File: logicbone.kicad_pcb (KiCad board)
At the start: 8 copper layers, 86.4 x 54.6 mm, 234 parts, among them IC1 ECP5UM-CABGA381, IC10 AT25SL128A, IC12 74LVC1G07, IC13 TPS51206, IC14 KSZ9031RNXCA, IC16 NCP349, IC17 NCP110AMX110, IC18 NCP110AMX110, IC19 NCP115AMX250, IC2 DDR3-TFBGA78, IC20 NCP115AMX250, IC3 DDR3-TFBGA78, IC4 MXL7704, IC5 PI6CG18401, IC7 FUSB302-QFN14, IC9 ADC120, J1 NGFF-KEY-E, J2 GCT_USB4110_USBC, J3 ARJM11xx-502, J4 TC2050-IDC-NL, J6 Micro_SD_MEM2075, P8 BB_2x23, P9 BB_2x23, Q1 Q_PMOS_GSD, SW1 SW_SPST, SW2 SW_SPST, Y1 25MHz

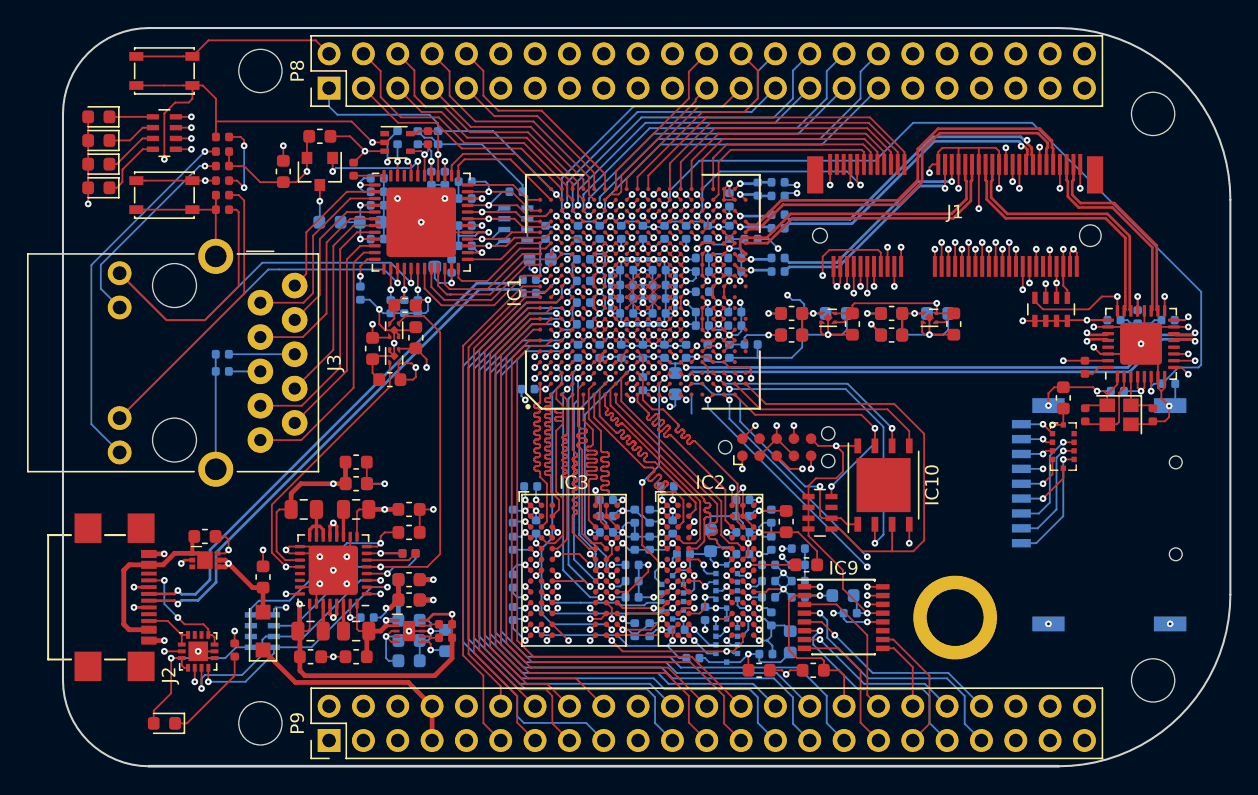
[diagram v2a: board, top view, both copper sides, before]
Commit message: Add a second USB-C port for USB host and SERDES breakout.
Now that the supervisor is gone, we have a bunch more PCB space which
we can use to add a USB-C downstream facing port that can serve as a
USB host and to breakout the extra SERDES channels.
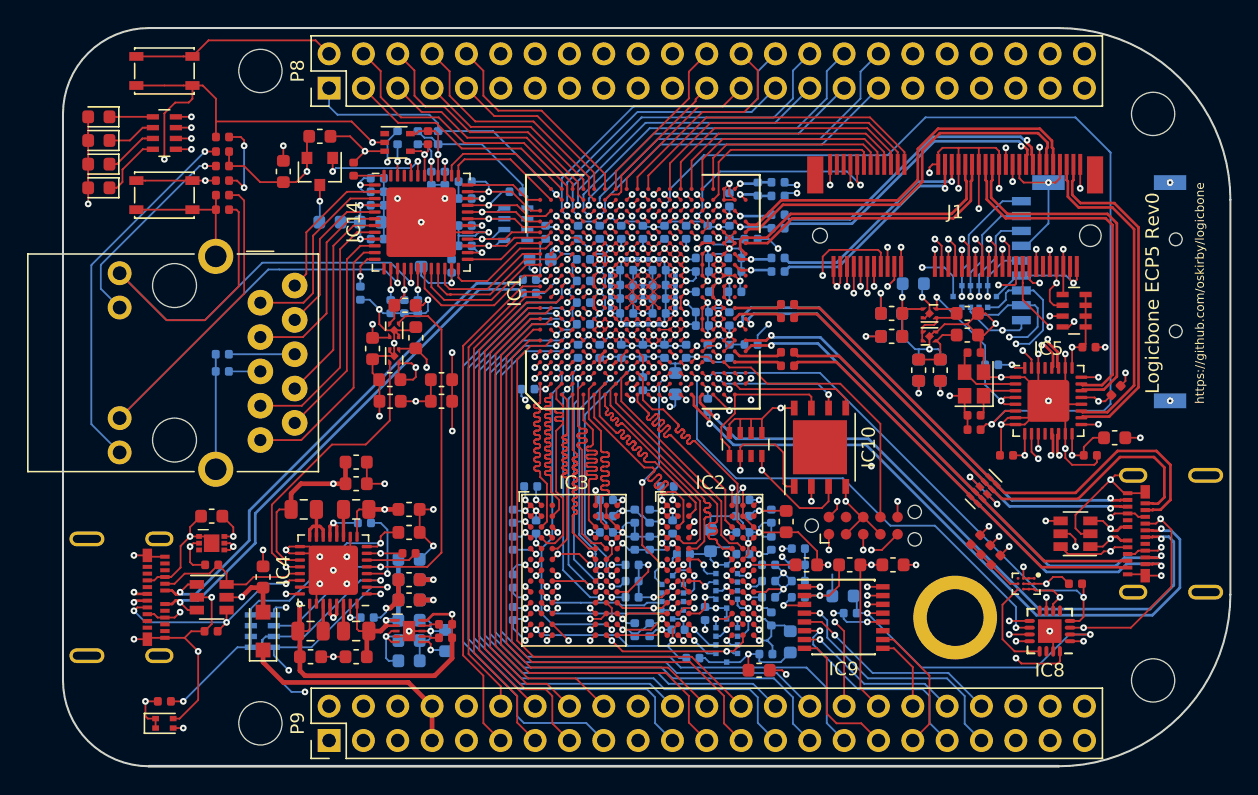
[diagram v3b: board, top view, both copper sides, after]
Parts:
- removed C119: 1uF, Capacitor_SMD:C_0603_1608Metric
- removed C250: 10uF, Capacitor_SMD:C_0603_1608Metric
- removed C252: 100nF, Capacitor_SMD:C_0402_1005Metric
- removed C253: 10nF, Capacitor_SMD:C_0402_1005Metric
- removed C254: 1nF, Capacitor_SMD:C_0402_1005Metric
- removed IC16: NCP349, Logicbone:DFN6_1.6x2mm
- added C10: 100nF, Capacitor_SMD:C_0402_1005Metric, F.Cu at (153.6, 66.8)
- added C101: 10uF, Capacitor_SMD:C_0603_1608Metric, F.Cu at (128.0, 71.4)
- added C102: 10uF, Capacitor_SMD:C_0603_1608Metric, B.Cu at (125.6, 84.7)
- added C11: 100nF, Capacitor_SMD:C_0402_1005Metric, F.Cu at (153.6, 65.8)
- added C3: 100nF, Capacitor_SMD:C_0402_1005Metric, B.Cu at (147.3, 66.4)
- added C4: 10nF, Capacitor_SMD:C_0402_1005Metric, B.Cu at (147.3, 67.4)
- added C5: 10uF, Capacitor_SMD:C_0603_1608Metric, B.Cu at (161.3, 68.2)
- added C6: 1nF, Capacitor_SMD:C_0402_1005Metric, B.Cu at (149.3, 66.9)
- added C7: 1uF, Capacitor_SMD:C_0603_1608Metric, F.Cu at (111.0, 81.5)
- added C8: 100nF, Capacitor_SMD:C_0402_1005Metric, F.Cu at (153.6, 70.4)
- added C9: 100nF, Capacitor_SMD:C_0402_1005Metric, F.Cu at (153.6, 69.4)
- added D10: TPD4E02B04, Package_SON:USON-10_2.5x1.0mm_P0.5mm, B.Cu at (168.1, 79.6)
- added D7: D5V0F4U6SO, Package_TO_SOT_SMD:SOT-23-6, F.Cu at (111.0, 87.5)
- added D8: D5V0F4U6SO, Package_TO_SOT_SMD:SOT-23-6, F.Cu at (174.9, 82.8)
- added D9: TPD4E02B04, Package_SON:USON-10_2.5x1.0mm_P0.5mm, F.Cu at (168.1, 79.6)
- added FB6: MPZ1608S600, Inductor_SMD:L_0603_1608Metric, F.Cu at (161.4, 85.1)
- added IC6: NCP349, Logicbone:DFN6_1.6x2mm, F.Cu at (111.0, 83.5)
- added IC8: FUSB307, Package_DFN_QFN:UQFN-16-1EP_3x3mm_P0.5mm_EP1.75x1.75mm, F.Cu at (173.0, 90.0)
- added J5: USB_C_Receptacle, Logicbone:Molex-1054500101, F.Cu at (179.2, 82.8)
- added R11: 5.1k, Resistor_SMD:R_0402_1005Metric, F.Cu at (111.0, 90.0)
- added R12: 5.1k, Resistor_SMD:R_0402_1005Metric, F.Cu at (111.0, 85.1)
- added R17: 1.5k, Resistor_SMD:R_0402_1005Metric, B.Cu at (147.7, 73.3)
- added R33: 750, Resistor_SMD:R_0402_1005Metric, F.Cu at (169.0, 84.8)
- added R34: 1.2k, Resistor_SMD:R_0402_1005Metric, F.Cu at (168.2, 84.0)
- added R35: 10k, Resistor_SMD:R_0402_1005Metric, F.Cu at (174.9, 86.5)
- added R36: 1.2k, Resistor_SMD:R_0402_1005Metric, F.Cu at (167.5, 83.2)
- C120, C121, C122, C123, C151, C171, R6: moved to F.Cu
- D1: value LED_ALT -> LED_Dual_ACAC; footprint LED_SMD:LED_0603_1608Metric -> KiCAD_Magic:LED_0603_DUAL
- IC7: value FUSB302-QFN14 -> FPF2595; footprint Package_DFN_QFN:WQFN-14-1EP_2.5x2.5mm_P0.5mm_EP1.45x1.45mm -> Logicbone:WLCSP-12_3x4_1.3x1.8mm
- J2: value GCT_USB4110_USBC -> USB_C_Receptacle; footprint Logicbone:USB4110 -> Logicbone:Molex-1054500101
- L1: value L -> 2.2uH
- L2, L4: value L -> 0.47uH
- L3: value L -> 1uH
- R8, RN10: moved to B.Cu
- moved IC7 61.5 mm to (171.2, 86.5), turned to 270 degrees
- moved C159 46.0 mm to (128.0, 73.0), turned to 0 degrees
- moved C165 21.1 mm to (177.8, 75.7), turned to 0 degrees
- moved J6 16.5 mm to (182.3, 65.0)
- moved R6 14.8 mm to (167.4, 75.1), turned to 0 degrees
- moved C122 14.1 mm to (169.8, 77.0), turned to 180 degrees
- moved C108 13.2 mm to (167.4, 74.0), turned to 180 degrees
- moved RN10 12.9 mm to (167.5, 65.2), turned to 0 degrees
- moved C529 11.8 mm to (164.9, 70.7), turned to 90 degrees
- moved FB3 11.8 mm to (164.9, 70.7), turned to 270 degrees
- moved Y1 11.0 mm to (167.4, 71.7), turned to 90 degrees
- moved C171 9.83 mm to (166.9, 68.1)
- moved C524 9.75 mm to (163.3, 70.7), turned to 90 degrees
- moved FB2 9.75 mm to (163.3, 70.7), turned to 270 degrees
- moved C109 9.42 mm to (167.4, 69.4), turned to 0 degrees
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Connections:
- net /FPGA Programming/FLASH_MISO renamed /USB and Programming/FLASH_MISO
- net /FPGA Programming/FLASH_MOSI renamed /USB and Programming/FLASH_MOSI
- net /FPGA Programming/FLASH_SCLK renamed /USB and Programming/FLASH_SCLK
- net /FPGA Programming/FPGA_DONE renamed /USB and Programming/FPGA_DONE
- net /FPGA Programming/FPGA_TCK renamed /USB and Programming/FPGA_TCK
- net /FPGA Programming/FPGA_TDI renamed /USB and Programming/FPGA_TDI
- net /FPGA Programming/FPGA_TDO renamed /USB and Programming/FPGA_TDO
- net /FPGA Programming/FPGA_TMS renamed /USB and Programming/FPGA_TMS
- net /FPGA Programming/~FLASH_CSEL renamed /USB and Programming/~FLASH_CSEL
- net /FPGA SERDES/VCCTRX0 renamed /USB and Programming/VCCTRX0
- C116 pad 1: VADC -> /Exp Headers/VADC
- C116 pad 2: GND -> GNDA
- C117 pad 1: VADC -> /Exp Headers/VADC
- C117 pad 2: GND -> GNDA
- C159 pad 1: VCC3V3 -> VCORE
- D1 pad 1: Net-(D1-Pad1) -> /FPGA Power/PGOOD
- D1 pad 2: +3V3 -> GND
- FB1 pad 1: VADC -> /Exp Headers/VADC
- IC1 pad D10: /Exp Headers/ADC_SCLK -> /Exp Headers/ADC_MOSI
- IC1 pad D13: /Ethernet/MMC_DAT2 -> /Ethernet/MMC_DAT0
- IC1 pad D14: /Ethernet/MMC_DAT1 -> /Ethernet/MMC_DET
- IC1 pad D15: /Ethernet/MMC_DAT3 -> /Ethernet/MMC_CMD
- IC1 pad E13: /Ethernet/MMC_DAT0 -> /Ethernet/MMC_DAT1
- IC1 pad E14: /Ethernet/MMC_CMD -> /Ethernet/MMC_DAT3
- IC1 pad E15: /Ethernet/MMC_DET -> /Ethernet/MMC_DAT2
- IC1 pad E8: /Exp Headers/ADC_MOSI -> /Exp Headers/ADC_SCLK
- IC1 pad L17: /FPGA SERDES/~M2_WDIS2 -> /FPGA SERDES/~M2_WDIS1
- IC1 pad L19: /FPGA SERDES/~M2_WDIS1 -> /FPGA SERDES/~M2_ALERT
- IC1 pad M17: /FPGA SERDES/~M2_ALERT -> /FPGA SERDES/~PCIE_RESET0
- IC1 pad M18: /FPGA SERDES/~PCIE_RESET0 -> /FPGA SERDES/~M2_WDIS2
- IC1 pad N18: /FPGA SERDES/M2_VEND2 -> /FPGA SERDES/M2_VEND0
- IC1 pad P17: /FPGA SERDES/M2_RTS -> /FPGA SERDES/M2_VEND2
- IC1 pad P18: /FPGA SERDES/M2_COEX2 -> /FPGA SERDES/M2_COEX1
- IC1 pad P19: /FPGA SERDES/M2_VEND1 -> /FPGA SERDES/M2_COEX2
- IC1 pad R1: Net-(IC1-PadR1) -> /USB and Programming/USB_DFP+
- IC1 pad R17: /FPGA SERDES/M2_TXD -> /FPGA SERDES/M2_RXD
- IC1 pad R3: /FPGA Programming/~USB_INT -> /USB and Programming/~USB_INT
- IC1 pad T1: Net-(IC1-PadT1) -> /USB and Programming/USB_DFP-
- IC1 pad T19: /FPGA SERDES/M2_COEX1 -> /FPGA SERDES/M2_VEND1
- IC1 pad T2: Net-(IC1-PadT2) -> /USB and Programming/USB_DFP_PULL
- IC1 pad T3: Net-(IC1-PadT3) -> /USB and Programming/USB_ORIENT
- IC1 pad U17: /FPGA SERDES/M2_RXD -> /FPGA SERDES/M2_TXD
- IC1 pad U18: /FPGA SERDES/M2_VEND0 -> /FPGA SERDES/M2_RTS
- IC1 pad V3: /FPGA Programming/~FPGA_INIT -> /USB and Programming/~FPGA_INIT
- IC1 pad W1: /FPGA Programming/FLASH_D3 -> /USB and Programming/FLASH_D3
- IC1 pad Y2: /FPGA Programming/FLASH_D2 -> /USB and Programming/FLASH_D2
- IC1 pad Y5: Net-(IC1-PadY5) -> /USB and Programming/USBSS_RX1+
- IC1 pad Y6: Net-(IC1-PadY6) -> /USB and Programming/USBSS_RX1-
- IC1 pad Y7: Net-(IC1-PadY7) -> /USB and Programming/USBSS_RX2+
- IC1 pad Y8: Net-(IC1-PadY8) -> /USB and Programming/USBSS_RX2-
- IC10 pad 3: /FPGA Programming/FLASH_D2 -> /USB and Programming/FLASH_D2
- IC10 pad 7: /FPGA Programming/FLASH_D3 -> /USB and Programming/FLASH_D3
- IC20 pad 3: /FPGA Power/PMIC_PG2 -> /FPGA Power/PGOOD
- IC4 pad 20: /FPGA Power/PMIC_PG2 -> /FPGA Power/PGOOD
- IC4 pad 21: Net-(IC4-Pad21) -> /FPGA Power/USB_UFP_CC1
- IC4 pad 22: Net-(IC4-Pad22) -> /FPGA Power/USB_UFP_CC2
- IC9 pad 2: VADC -> /Exp Headers/VADC
- J2 pad A4: Net-(C119-Pad1) -> Net-(C7-Pad1)
- J2 pad A5: /FPGA Programming/USB_CC1 -> /FPGA Power/USB_UFP_CC1
- J2 pad A9: Net-(C119-Pad1) -> Net-(C7-Pad1)
- J2 pad B5: /FPGA Programming/USB_CC2 -> /FPGA Power/USB_UFP_CC2
- P9 pad 32: VADC -> VCC1V8
- R10 pad 1: /FPGA Programming/~FPGA_INIT -> /FPGA Power/PGOOD
- R10 pad 2: Net-(D1-Pad1) -> +3V3
- RN10 pad 3: /Ethernet/MMC_CMD -> /Ethernet/MMC_DAT2
- RN10 pad 5: /Ethernet/MMC_DAT2 -> /Ethernet/MMC_CMD
- RN5 pad 1: /FPGA Power/PMIC_PG2 -> /FPGA Power/PGOOD
- RN7 pad 1: /FPGA Programming/FLASH_D2 -> /USB and Programming/FLASH_D3
- RN7 pad 4: /FPGA Programming/FLASH_D3 -> /USB and Programming/FLASH_D2
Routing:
- net GND: track 1121.2 -> 1330.4 mm, vias 137 -> 151
- net /FPGA Programming/~USB_INT: track 69.1 -> 0.00 mm, vias 2 -> 0
- net /USB and Programming/~FPGA_INIT: track 0.00 -> 68.6 mm, vias 0 -> 2
- net VBUS: track 60.4 -> 124.9 mm, vias 5 -> 7
- net /USB and Programming/USB_DFP+: track 0.00 -> 58.9 mm, vias 0 -> 3
- net /USB and Programming/USB_DFP-: track 0.00 -> 55.8 mm, vias 0 -> 3
- net /FPGA Programming/~FPGA_INIT: track 52.2 -> 0.00 mm, vias 2 -> 0
- net /FPGA Power/PGOOD: track 0.00 -> 43.2 mm, vias 0 -> 3
- net /USB and Programming/USBSS_TX2-: track 0.00 -> 40.1 mm
- net /USB and Programming/USBSS_RX1+: track 0.00 -> 39.6 mm, vias 0 -> 2
- net /USB and Programming/USBSS_RX1-: track 0.00 -> 39.6 mm, vias 0 -> 2
- net /USB and Programming/USB_ORIENT: track 0.00 -> 39.0 mm, vias 0 -> 2
- net /USB and Programming/USBSS_TX2+: track 0.00 -> 38.6 mm
- net /USB and Programming/~USB_INT: track 0.00 -> 36.4 mm, vias 0 -> 2
- net /USB and Programming/USBSS_RX2+: track 0.00 -> 36.0 mm, vias 0 -> 2
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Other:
- net class USBSS added: clearance 0.08, trace_width 0.135, via_dia 0.5, via_drill 0.2
- board text added: "Logicbone ECP5 Rev0"
- board text added: "https://github.com/oskirby/logicbone"

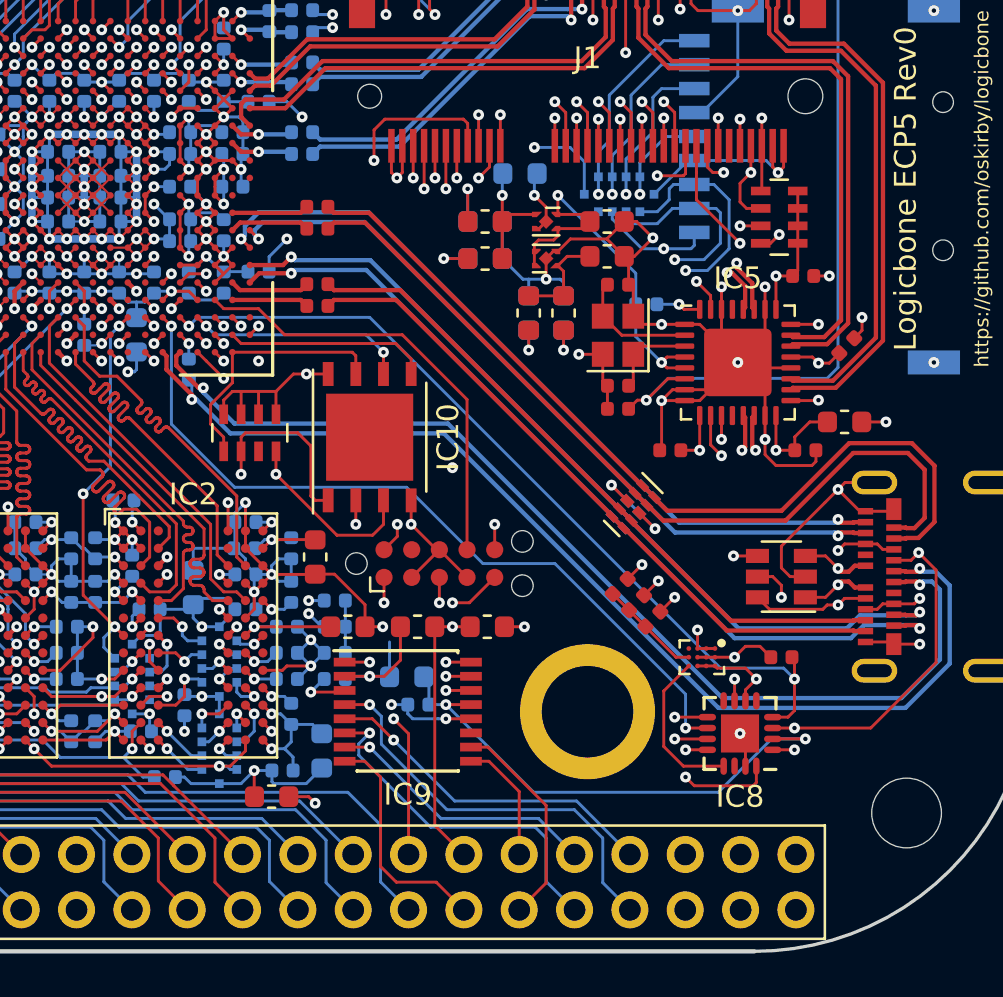
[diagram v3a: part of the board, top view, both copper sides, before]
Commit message: Replace ADC with a TLA2518
The previous ADC (STMicor ADC120) was only available in a TSSOP
package, which was unfortunately too tall to clear a double-sided
M.2 adaptor card. The TLA2518 comes in a WQFN16 package which is
much shorter.
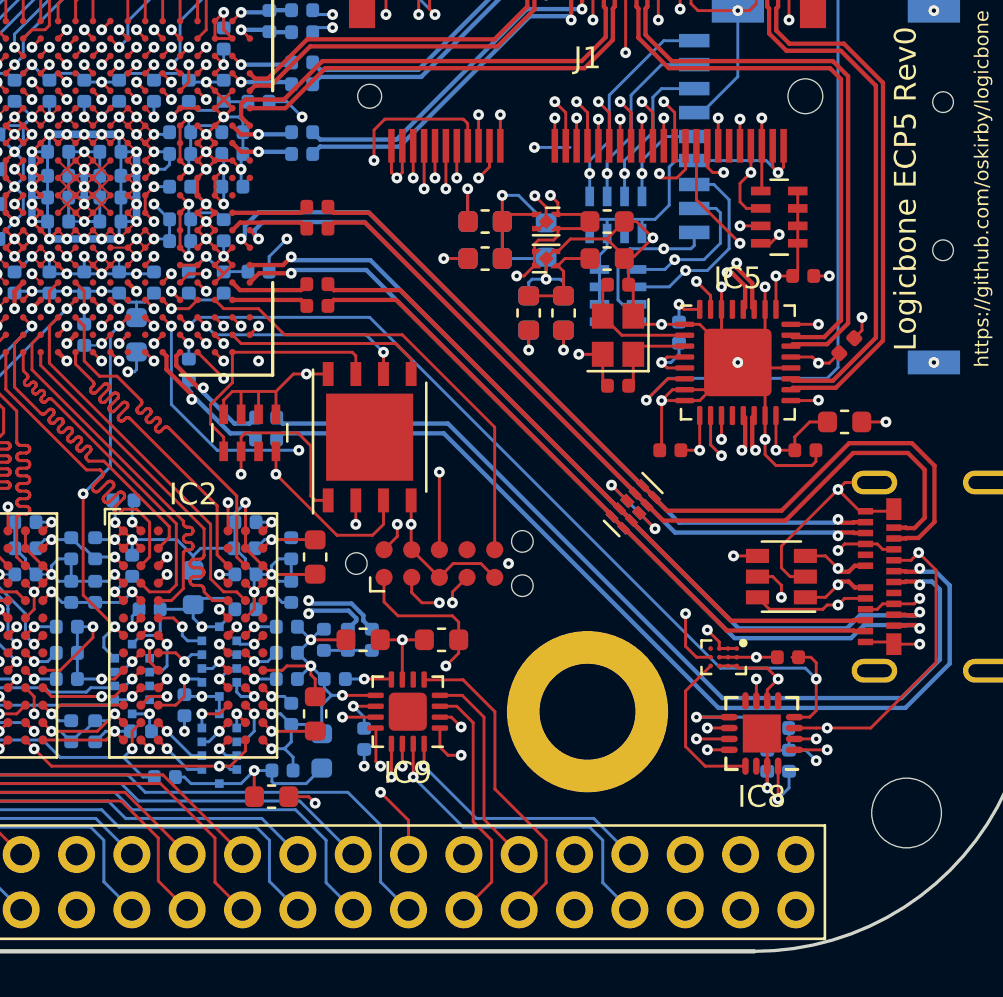
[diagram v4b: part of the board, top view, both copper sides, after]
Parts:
- removed FB6: MPZ1608S600, Inductor_SMD:L_0603_1608Metric
- removed RN10: 10k, KiCAD_Magic:EXBD-1206
- added R37: 20, Resistor_SMD:R_0402_1005Metric, B.Cu at (151.2, 75.5)
- added RN6: 10k, Resistor_SMD:R_Array_Concave_4x0603, B.Cu at (167.3, 66.2)
- added RN8: 10k, Resistor_SMD:R_Array_Concave_4x0603, B.Cu at (167.4, 69.9)
- FB1: moved to F.Cu
- H5: footprint KiCAD_Magic:Keystone-4881 -> Logicbone:wurth-9774025360
- IC9: value ADC120 -> TLA2518; footprint Package_SO:SSOP-16_4.4x5.2mm_P0.65mm -> Package_DFN_QFN:WQFN-16-1EP_3x3mm_P0.5mm_EP1.75x1.75mm
- R33, R34, R36: moved to B.Cu
- R6: value 10k -> 20; moved to B.Cu
- R7: value R_Small -> 12.1k
- moved R6 16.2 mm to (151.2, 76.5)
- moved R36 10.5 mm to (174.2, 91.2), turned to 90 degrees
- moved R34 10.1 mm to (175.2, 91.2), turned to 90 degrees
- moved R33 7.62 mm to (174.8, 89.8), turned to 0 degrees
- moved C420 4.27 mm to (153.5, 89.1), turned to 90 degrees
- moved C170 3.28 mm to (164.1, 67.3), turned to 270 degrees
- moved C118 2.94 mm to (155.8, 90.2), turned to 270 degrees
- moved C117 2.57 mm to (155.7, 85.7), turned to 180 degrees
- moved R15 2.48 mm to (156.1, 85.7), turned to 90 degrees
- moved FB1 2.33 mm to (159.3, 85.7)
- moved R8 1.98 mm to (170.2, 71.6), turned to 90 degrees
- moved IC7 1.00 mm to (172.2, 86.5)
- moved IC8 1.00 mm to (174.0, 90.0)
- moved R16 0.85 mm to (155.0, 85.7), turned to 270 degrees
- moved C469 0.78 mm to (153.9, 85.7), turned to 90 degrees
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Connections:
- C116 pad 1: /Exp Headers/VADC -> Net-(C116-Pad1)
- C116 pad 2: GNDA -> GND
- C117 pad 1: /Exp Headers/VADC -> Net-(C117-Pad1)
- C117 pad 2: GNDA -> GND
- D8 pad 1: /USB and Programming/USB_DFP+ -> /USB and Programming/USBC_DFP+
- D8 pad 3: /USB and Programming/USB_DFP- -> /USB and Programming/USBC_DFP-
- FB1 pad 1: /Exp Headers/VADC -> Net-(C117-Pad1)
- IC1 pad E8: /Exp Headers/ADC_SCLK -> /Exp Headers/ADC_MISO
- IC1 pad E9: /Exp Headers/ADC_MISO -> /Exp Headers/ADC_SCLK
- IC1 pad R1: /USB and Programming/USB_DFP+ -> /USB and Programming/FPGA_USB_DFP+
- IC1 pad T1: /USB and Programming/USB_DFP- -> /USB and Programming/FPGA_USB_DFP-
- IC9 pad 1: /Exp Headers/~ADC_CSEL -> /Exp Headers/P9_AIN2
- IC9 pad 10: /Exp Headers/P9_AIN6 -> VCC3V3
- IC9 pad 11: Net-(IC9-Pad11) -> /Exp Headers/~ADC_CSEL
- IC9 pad 12: GND -> /Exp Headers/ADC_MISO
- IC9 pad 13: VCC3V3 -> /Exp Headers/ADC_SCLK
- IC9 pad 15: /Exp Headers/ADC_MISO -> /Exp Headers/P9_AIN0
- IC9 pad 16: /Exp Headers/ADC_SCLK -> /Exp Headers/P9_AIN1
- IC9 pad 2: /Exp Headers/VADC -> /Exp Headers/P9_AIN3
- IC9 pad 3: GNDA -> /Exp Headers/P9_AIN4
- IC9 pad 4: /Exp Headers/P9_AIN0 -> /Exp Headers/P9_AIN5
- IC9 pad 5: /Exp Headers/P9_AIN1 -> /Exp Headers/P9_AIN6
- IC9 pad 6: /Exp Headers/P9_AIN2 -> Net-(IC9-Pad6)
- IC9 pad 7: /Exp Headers/P9_AIN3 -> Net-(C117-Pad1)
- IC9 pad 8: /Exp Headers/P9_AIN4 -> Net-(C116-Pad1)
- IC9 pad 9: /Exp Headers/P9_AIN5 -> GND
- J4 pad 1: /USB and Programming/FPGA_TCK -> VCC3V3
- J4 pad 2: GND -> /USB and Programming/FPGA_TMS
- J4 pad 3: /USB and Programming/FPGA_TMS -> GND
- J4 pad 4: GND -> /USB and Programming/FPGA_TCK
- J4 pad 5: /USB and Programming/FPGA_TDI -> GND
- J4 pad 6: VCC3V3 -> /USB and Programming/FPGA_TDO
- J4 pad 7: /USB and Programming/FPGA_TDO -> Net-(J4-Pad7)
- J4 pad 8: GND -> /USB and Programming/FPGA_TDI
- J4 pad 9: Net-(J4-Pad9) -> GND
- J5 pad A6: /USB and Programming/USB_DFP+ -> /USB and Programming/USBC_DFP+
- J5 pad A7: /USB and Programming/USB_DFP- -> /USB and Programming/USBC_DFP-
- J5 pad B6: /USB and Programming/USB_DFP+ -> /USB and Programming/USBC_DFP+
- J5 pad B7: /USB and Programming/USB_DFP- -> /USB and Programming/USBC_DFP-
- P9 pad 34: GNDA -> GND
- R17 pad 2: /USB and Programming/USB_DFP+ -> /USB and Programming/FPGA_USB_DFP+
- R6 pad 1: GND -> /USB and Programming/FPGA_USB_DFP+
- R6 pad 2: /Ethernet/25M_REFCLK -> /USB and Programming/USBC_DFP+
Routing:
- net /USB and Programming/USB_DFP+: track 58.9 -> 0.00 mm, vias 3 -> 0
- net /USB and Programming/USB_DFP-: track 55.8 -> 0.00 mm, vias 3 -> 0
- net /USB and Programming/USBC_DFP+: track 0.00 -> 50.8 mm, vias 0 -> 2
- net /USB and Programming/USBC_DFP-: track 0.00 -> 49.4 mm, vias 0 -> 2
- net GNDA: track 22.8 -> 0.00 mm, vias 2 -> 0
- net Net-(IC8-Pad16): track 15.1 -> 2.97 mm, vias 2 -> 1
- net Net-(IC7-PadD2): track 4.70 -> 15.6 mm, vias 0 -> 2
- net /Exp Headers/VADC: track 8.24 -> 0.00 mm, vias 1 -> 0
- net /USB and Programming/FPGA_USB_DFP+: track 0.00 -> 7.53 mm, vias 0 -> 1
- net /Exp Headers/ADC_SCLK: track 39.4 -> 46.1 mm
- net VCC1V8: track 213.2 -> 206.7 mm, vias 11 -> 12
- net /Exp Headers/ADC_MISO: track 40.0 -> 46.1 mm
- net /USB and Programming/FPGA_USB_DFP-: track 0.00 -> 5.66 mm, vias 0 -> 1
- net /Exp Headers/P9_AIN2: track 16.4 -> 11.3 mm
- net VCCAUXTRX: track 57.1 -> 62.3 mm
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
